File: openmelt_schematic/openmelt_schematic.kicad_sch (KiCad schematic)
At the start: 11 parts, among them M1 Motor_DC, U1 A000053

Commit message: documentaion
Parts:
- added BT1: 7.4v Lipo Battery, symbol Device:Battery
- D2: value DIODE -> Schottky Diode 30A (30SQ050)
- U1: value A000053 -> Arduino Micro
- gave numbers to parts that had none: 3
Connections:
- net +BATT: now also BT1.1 (+)
- net -BATT renamed GND
- net GND: now also BT1.2 (-)
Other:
- note added: "(MOTOR_2 goes to 2nd MOSFET / motor for 2 wheeled bot)"
- note added: "(incorporates 5v <-> 3v level shifter)"
- note removed: "Adafruit incorporates 5v <-> 3v level shifter. Sparkfun board may alternately be used in conjuction with level shifter breakout. TODO: More info"
- moved on the sheet: C1, D1, D2, M1, Q1, R1, R2, R3, U1, U2, U3

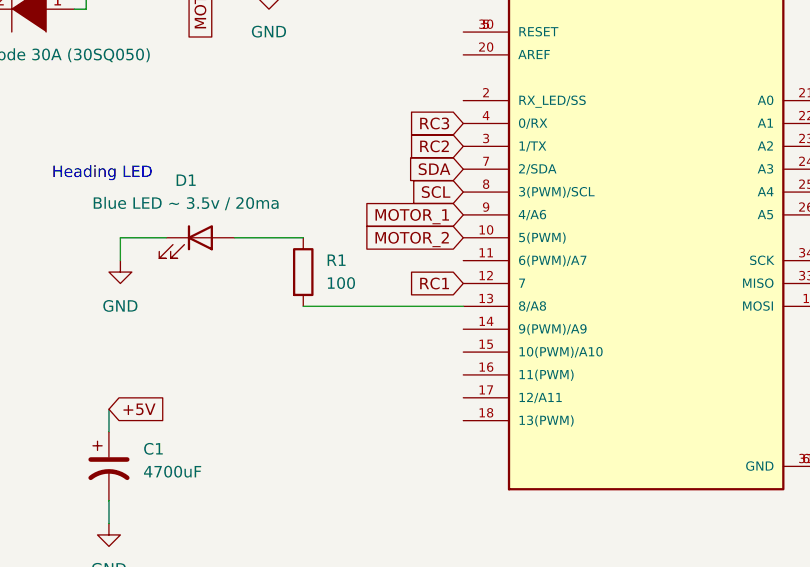
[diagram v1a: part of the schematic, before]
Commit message: fixing error in schematic
MOTOR_1 and MOTOR_2 were incorrect!
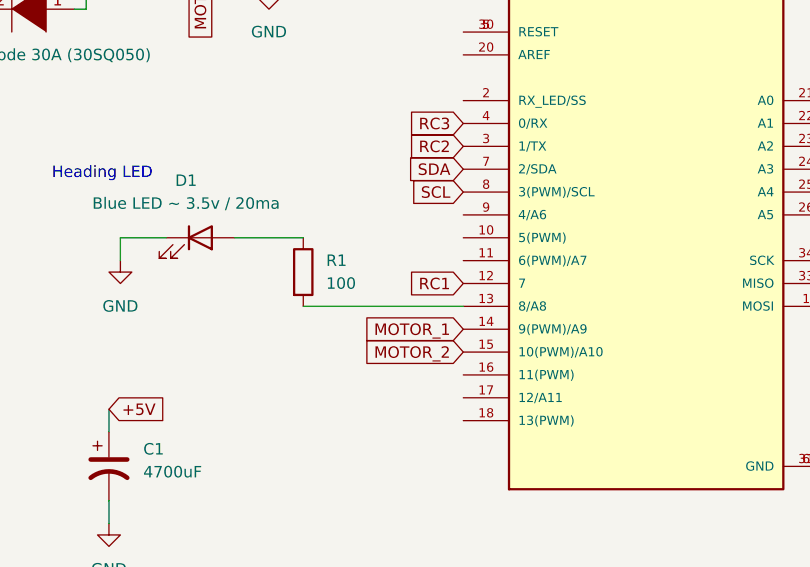
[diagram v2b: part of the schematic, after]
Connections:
- net MOTOR_1: now also U1.14 (9(PWM)/A9); no longer U1.9 (4/A6)
- net MOTOR_2: now also U1.15 (10(PWM)/A10); no longer U1.10 (5(PWM))
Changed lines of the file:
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@@
     (effects (font (size 1.27 1.27)) (justify left bottom))
+  )
+  (global_label "MOTOR_1" (shape input) (at 91.44 95.25 180) (fields_autoplaced)
+    (effects (font (size 1.27 1.27)) (justify right))
+    (property "Intersheet References" "${INTERSHEET_REFS}" (id 0) (at 80.4998 95.1706 0)
+      (effects (font (size 1.27 1.27)) (justify right) hide)
+    )
   )
   (global_label "+5V" (shape input) (at 52.07 104.14 0) (fields_autoplaced)
@@
     )
   )
-  (global_label "MOTOR_1" (shape input) (at 91.44 82.55 180) (fields_autoplaced)
+  (global_label "MOTOR_2" (shape input) (at 91.44 97.79 180) (fields_autoplaced)
     (effects (font (size 1.27 1.27)) (justify right))
-    (property "Intersheet References" "${INTERSHEET_REFS}" (id 0) (at 80.4998 82.4706 0)
+    (property "Intersheet References" "${INTERSHEET_REFS}" (id 0) (at 80.4998 97.7106 0)
       (effects (font (size 1.27 1.27)) (justify right) hide)
     )
@@
     )
   )
-  (global_label "MOTOR_2" (shape input) (at 91.44 85.09 180) (fields_autoplaced)
-    (effects (font (size 1.27 1.27)) (justify right))
-    (property "Intersheet References" "${INTERSHEET_REFS}" (id 0) (at 80.4998 85.0106 0)
-      (effects (font (size 1.27 1.27)) (justify right) hide)
-    )
-  )
